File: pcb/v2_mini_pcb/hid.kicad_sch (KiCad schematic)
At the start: 8 parts, among them U4 LP5813ADRRR

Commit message: add input buttons
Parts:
- added SW3, SW4, SW5, SW6: SW_Push, Button_Switch_SMD:SW_SPST_B3U-1000P, symbol Switch:SW_Push
- added U5: TCA9536ADTMR, all:X2SON8_DTM_TEX, symbol all:TCA9536ADTMR
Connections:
- net +3V3: now also U5.7 (VCC)
- net GND: now also SW3.1, SW4.1, SW5.1, SW6.2, U5.3 (GND)
- net HDI_SCL: now also U5.5 (SCL)
- net HDI_SDA: now also U5.6 (SDA)
- new net: SW5.2, U5.4 (P3/INT)
- new net: SW3.2, U5.1 (P0)
- new net: SW4.2, U5.2 (P2)
- new net: SW6.1, U5.8 (P1)

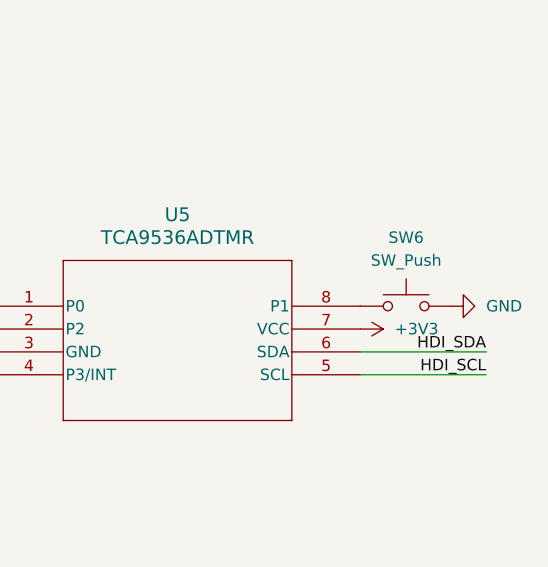
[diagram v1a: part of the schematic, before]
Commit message: fix input buttons
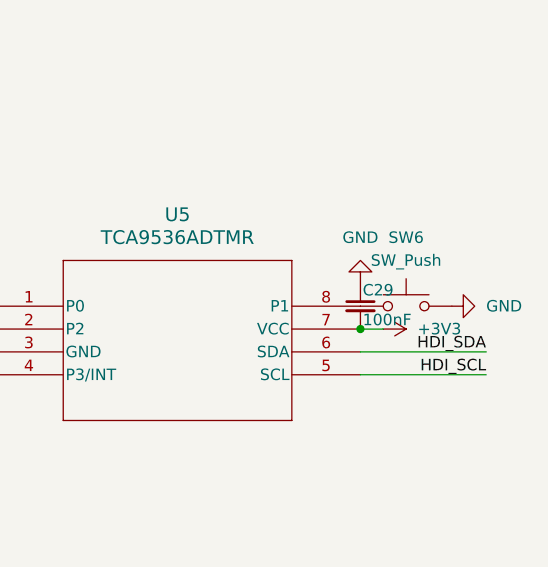
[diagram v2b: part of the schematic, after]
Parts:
- added C29: 100nF, symbol Device:C_Small
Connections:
- net +3V3: now also C29.2
- net GND: now also C29.1
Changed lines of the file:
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@@
 	)
 	(junction
+		(at 256.54 57.15)
+		(diameter 0)
+		(color 0 0 0 0)
+	)
+	(junction
 		(at 111.76 72.39)
 		(diameter 0)
@@
 	(wire
 		(pts
+			(xy 259.08 57.15) (xy 256.54 57.15)
+		)
+		(stroke
+			(width 0)
+			(type default)
+		)
+	)
+	(wire
+		(pts
 			(xy 133.35 114.3) (xy 138.43 114.3)
 		)
@@
 	)
 	(symbol
+		(lib_id "Device:C_Small")
+		(at 256.54 54.61 0)
+		(unit 1)
+		(body_style 1)
+		(exclude_from_sim no)
+		(in_bom yes)
+		(on_board yes)
+		(in_pos_files yes)
+		(dnp no)
+		(property "Reference" "C29"
+			(at 256.794 52.832 0)
+			(show_name no)
+			(do_not_autoplace no)
+			(effects
+				(font
+					(size 1.27 1.27)
+				)
+				(justify left)
+			)
+		)
+		(property "Value" "100nF"
+			(at 256.794 56.134 0)
+			(show_name no)
+			(do_not_autoplace no)
+			(effects
+				(font
+					(size 1.27 1.27)
+				)
+				(justify left)
+			)
+		)
+		(property "Footprint" ""
+			(at 256.54 54.61 0)
+			(hide yes)
+			(show_name no)
+			(do_not_autoplace no)
+			(effects
+				(font
+					(size 1.27 1.27)
+				)
+			)
+		)
+		(property "Datasheet" ""
+			(at 256.54 54.61 0)
+			(hide yes)
+			(show_name no)
+			(do_not_autoplace no)
+			(effects
+				(font
+					(size 1.27 1.27)
+				)
+			)
+		)
+		(property "Description" "Unpolarized capacitor, small symbol"
+			(at 256.54 54.61 0)
+			(hide yes)
+			(show_name no)
+			(do_not_autoplace no)
+			(effects
+				(font
+					(size 1.27 1.27)
+				)
+			)
+		)
+		(pin "2"
+		)
+		(pin "1"
+		)
+		(instances
+			(project "v2_mini"
+				(path "/4318b369-034c-40ef-a05b-b7d2541c0647/7336fb98-a0f9-496a-8177-e3e3b101e734"
+					(reference "C29")
+					(unit 1)
+				)
+			)
+		)
+	)
+	(symbol
 		(lib_id "power:+3V3")
 		(at 31.75 68.58 0)
@@
 	)
 	(symbol
+		(lib_id "power:GND")
+		(at 256.54 52.07 0)
+		(mirror x)
+		(unit 1)
+		(body_style 1)
+		(exclude_from_sim no)
+		(in_bom yes)
+		(on_board yes)
+		(in_pos_files yes)
+		(dnp no)
+		(fields_autoplaced yes)
+		(property "Reference" "#PWR088"
+			(at 256.54 45.72 0)
+			(hide yes)
+			(show_name no)
+			(do_not_autoplace no)
+			(effects
+				(font
+					(size 1.27 1.27)
+				)
+			)
+		)
+		(property "Value" "GND"
+			(at 256.54 46.99 0)
+			(show_name no)
+			(do_not_autoplace no)
+			(effects
+				(font
+					(size 1.27 1.27)
+				)
+			)
+		)
+		(property "Footprint" ""
+			(at 256.54 52.07 0)
+			(hide yes)
+			(show_name no)
+			(do_not_autoplace no)
+			(effects
+				(font
+					(size 1.27 1.27)
+				)
+			)
+		)
+		(property "Datasheet" ""
+			(at 256.54 52.07 0)
+			(hide yes)
+			(show_name no)
+			(do_not_autoplace no)
+			(effects
+				(font
+					(size 1.27 1.27)
+				)
+			)
+		)
+		(property "Description" "Power symbol creates a global label with name \"GND\" , ground"
+			(at 256.54 52.07 0)
+			(hide yes)
+			(show_name no)
+			(do_not_autoplace no)
+			(effects
+				(font
+					(size 1.27 1.27)
+				)
+			)
+		)
+		(pin "1"
+		)
+		(instances
+			(project "v2_mini"
+				(path "/4318b369-034c-40ef-a05b-b7d2541c0647/7336fb98-a0f9-496a-8177-e3e3b101e734"
+					(reference "#PWR088")
+					(unit 1)
+				)
+			)
+		)
+	)
+	(symbol
 		(lib_id "all:TCA9536ADTMR")
 		(at 215.9 54.61 0)
@@
 	(symbol
 		(lib_id "power:+3V3")
-		(at 256.54 57.15 270)
+		(at 259.08 57.15 270)
 		(mirror x)
 		(unit 1)
@@
 		(fields_autoplaced yes)
 		(property "Reference" "#PWR082"
-			(at 252.73 57.15 0)
+			(at 255.27 57.15 0)
 			(hide yes)
 			(show_name no)
@@
 		)
 		(property "Value" "+3V3"
-			(at 260.35 57.1499 90)
+			(at 262.89 57.1499 90)
 			(show_name no)
 			(do_not_autoplace no)
@@
 		)
 		(property "Footprint" ""
-			(at 256.54 57.15 0)
+			(at 259.08 57.15 0)
 			(hide yes)
 			(show_name no)
@@
 		)
 		(property "Datasheet" ""
-			(at 256.54 57.15 0)
+			(at 259.08 57.15 0)
 			(hide yes)
 			(show_name no)
@@
 		)
 		(property "Description" "Power symbol creates a global label with name \"+3V3\""
-			(at 256.54 57.15 0)
+			(at 259.08 57.15 0)
 			(hide yes)
 			(show_name no)

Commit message: finish gnss part of pcb
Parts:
- C29: footprint (none) -> Capacitor_SMD:C_0402_1005Metric; MPN (none) -> CL05B104KO5NNNC
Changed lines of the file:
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@@
 			)
 		)
-		(property "Footprint" ""
+		(property "Footprint" "Capacitor_SMD:C_0402_1005Metric"
 			(at 256.54 54.61 0)
 			(hide yes)
@@
 			(at 256.54 54.61 0)
 			(hide yes)
+			(show_name no)
+			(do_not_autoplace no)
+			(effects
+				(font
+					(size 1.27 1.27)
+				)
+			)
+		)
+		(property "MPN" "CL05B104KO5NNNC"
+			(at 256.54 54.61 0)
+			(hide yes)

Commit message: update bom
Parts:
- C27: DigiKey_PN (none) -> 1276-CL10A106KP8NNNDCT-ND; JLCPCB_PN C19702 -> (none); LCSC C19702 -> (none); MPN CL10A106KP8NNNC -> CL10A106KP8NNND; Supplier JLCPCB Basic -> DigiKey
- C28: DigiKey_PN (none) -> 311-1903-1-ND; JLCPCB_PN C45783 -> (none); LCSC C45783 -> (none); MPN CL21A226MAQNNNE -> CC0805MKX5R8BB226; Manufacturer Samsung Electro-Mechanics -> YAGEO; Supplier JLCPCB Basic -> DigiKey
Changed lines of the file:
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@@
 			)
 		)
-		(property "Datasheet" ""
+		(property "Datasheet" "https://product.samsungsem.com/mlcc/CL10A106KP8NNN.do"
 			(at 38.1 66.04 0)
 			(hide yes)
@@
 			)
 		)
-		(property "MPN" "CL10A106KP8NNNC"
+		(property "MPN" "CL10A106KP8NNND"
 			(at 38.1 66.04 0)
 			(hide yes)
@@
 			)
 		)
-		(property "LCSC" "C19702"
-			(at 38.1 66.04 0)
-			(hide yes)
-			(show_name no)
-			(do_not_autoplace no)
-			(effects
-				(font
-					(size 1.27 1.27)
-				)
-			)
-		)
-		(property "JLCPCB_PN" "C19702"
-			(at 38.1 66.04 0)
-			(hide yes)
-			(show_name no)
-			(do_not_autoplace no)
-			(effects
-				(font
-					(size 1.27 1.27)
-				)
-			)
-		)
-		(property "Supplier" "JLCPCB Basic"
+		(property "Supplier" "DigiKey"
 			(at 38.1 66.04 0)
 			(hide yes)
@@
 			)
 		)
+    (property "DigiKey_PN" "1276-CL10A106KP8NNNDCT-ND" (at 38.1 66.04 0)
+      (effects (font (size 1.27 1.27)) (hide yes))
+    )
 		(pin "1"
 		)
@@
 			)
 		)
-		(property "Datasheet" ""
+		(property "Datasheet" "https://yageogroup.com/download/specsheet/CC0805MKX5R8BB226"
 			(at 82.55 67.31 0)
 			(hide yes)
@@
 			)
 		)
-		(property "MPN" "CL21A226MAQNNNE"
-			(at 82.55 67.31 0)
-			(hide yes)
-			(show_name no)
-			(do_not_autoplace no)
-			(effects
-				(font
-					(size 1.27 1.27)
-				)
-			)
-		)
-		(property "Manufacturer" "Samsung Electro-Mechanics"
-			(at 82.55 67.31 0)
-			(hide yes)
-			(show_name no)
-			(do_not_autoplace no)
-			(effects
-				(font
-					(size 1.27 1.27)
-				)
-			)
-		)
-		(property "LCSC" "C45783"
-			(at 82.55 67.31 0)
-			(hide yes)
-			(show_name no)
-			(do_not_autoplace no)
-			(effects
-				(font
-					(size 1.27 1.27)
-				)
-			)
-		)
-		(property "JLCPCB_PN" "C45783"
-			(at 82.55 67.31 0)
-			(hide yes)
-			(show_name no)
-			(do_not_autoplace no)
-			(effects
-				(font
-					(size 1.27 1.27)
-				)
-			)
-		)
-		(property "Supplier" "JLCPCB Basic"
+		(property "MPN" "CC0805MKX5R8BB226"
+			(at 82.55 67.31 0)
+			(hide yes)
+			(show_name no)
+			(do_not_autoplace no)
+			(effects
+				(font
+					(size 1.27 1.27)
+				)
+			)
+		)
+		(property "Manufacturer" "YAGEO"
+			(at 82.55 67.31 0)
+			(hide yes)
+			(show_name no)
+			(do_not_autoplace no)
+			(effects
+				(font
+					(size 1.27 1.27)
+				)
+			)
+		)
+		(property "Supplier" "DigiKey"
 			(at 82.55 67.31 0)
 			(hide yes)
@@
 			)
 		)
+    (property "DigiKey_PN" "311-1903-1-ND" (at 82.55 67.31 0)
+      (effects (font (size 1.27 1.27)) (hide yes))
+    )
 		(pin "1"
 		)
